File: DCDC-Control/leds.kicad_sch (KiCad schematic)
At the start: 4 parts

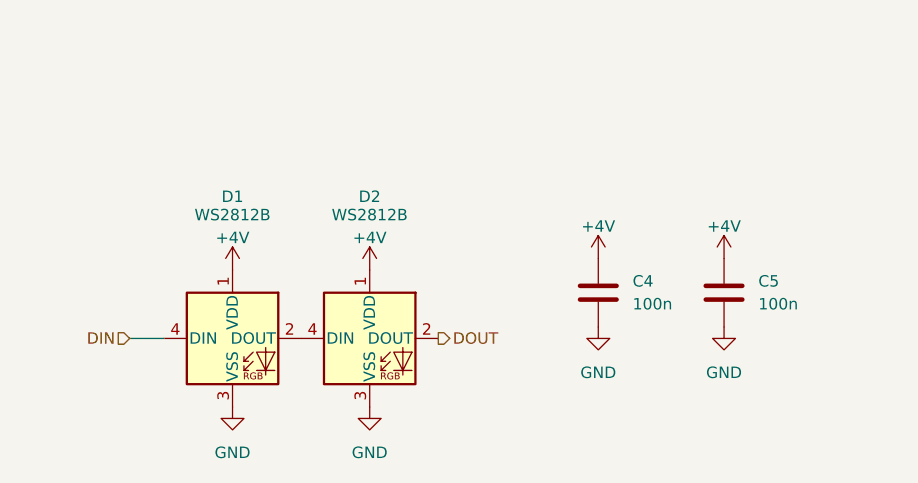
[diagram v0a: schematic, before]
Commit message: some DCDC schematics
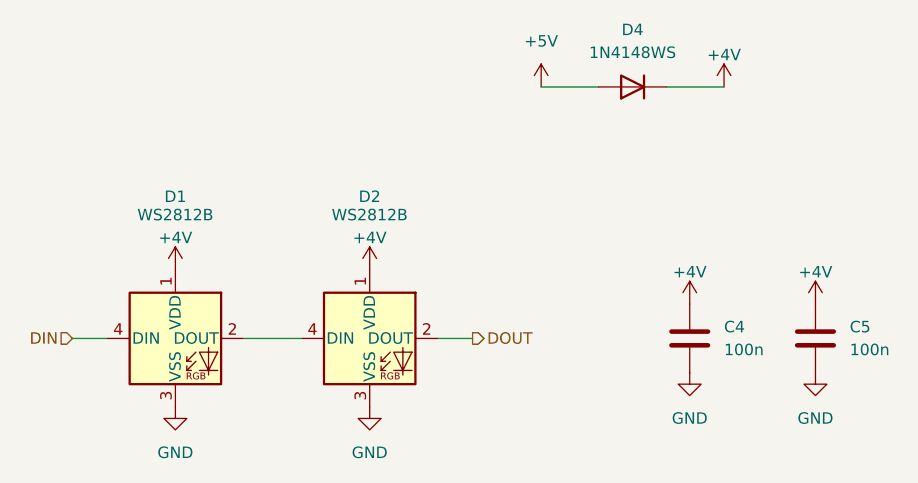
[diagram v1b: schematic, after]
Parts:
- added D4: 1N4148WS, Diode_SMD:D_SOD-323, symbol Diode:1N4148WS
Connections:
- net +4V: now also D4.1 (K)
- new net +5V: D4.2 (A)
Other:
- moved on the sheet: C4, C5, D1
